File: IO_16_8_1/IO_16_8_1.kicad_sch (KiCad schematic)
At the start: 76 parts, among them J1 Conn_01x06, J2 nmount JST 1mm QWIIC, J3 nmount SW Debug, J4 USB_C_Receptacle_USB2.0, J5 Conn_01x06, SW1 Reset, SW2 Boot, SW3 SW_DIP_x04, U1 ADM3483, U2 W25Q32JVSS, U3 RP2040, U4 LMV321, U5 SN74AHCT1G125, U6 AP2112K-3.3, Y1 12MHz,18pF

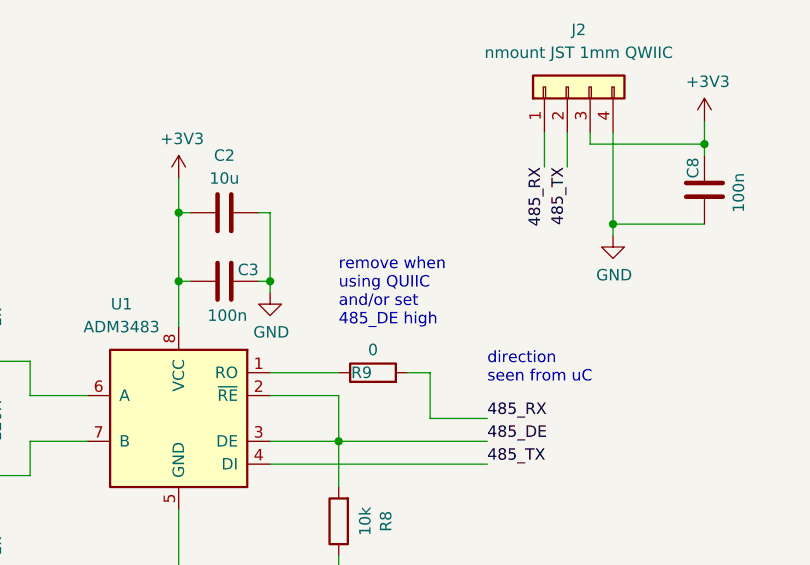
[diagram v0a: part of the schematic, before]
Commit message: fixed typo QUIIC -> QWIIC
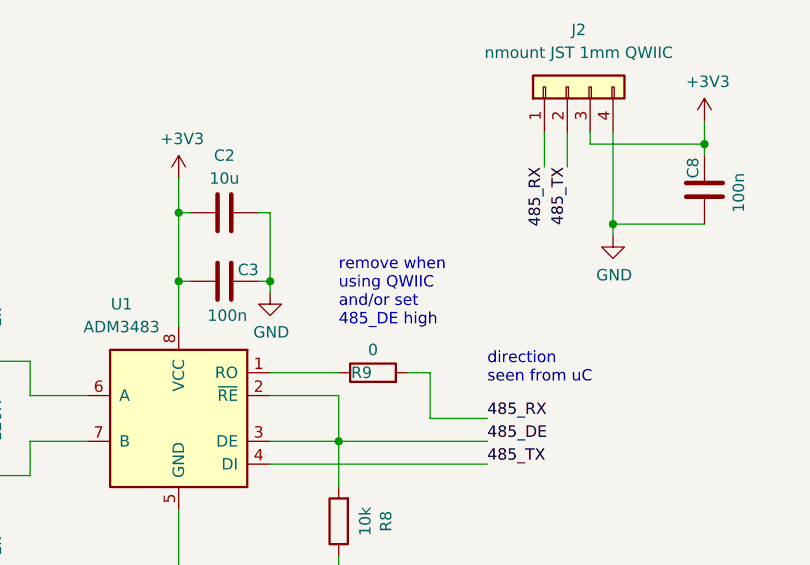
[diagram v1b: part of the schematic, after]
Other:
- note added: "remove when using QWIIC and/or set 485_DE high"
- note removed: "remove when using QUIIC and/or set 485_DE high"
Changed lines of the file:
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@@
     (effects (font (size 5 5) bold) (justify left bottom))
   )
-  (text "remove when\nusing QUIIC\nand/or set\n485_DE high" (at 105.41 50.8 0)
+  (text "remove when\nusing QWIIC\nand/or set\n485_DE high" (at 105.41 50.8 0)
     (effects (font (size 1.27 1.27)) (justify left bottom))
   )

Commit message: changed In_1, In_2
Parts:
- added R96, R97: 10k, symbol Device:R
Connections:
- net +3V3: now also R96.1, R97.1
- net 485_RX: now also R96.2
- net 485_TX: now also R97.2
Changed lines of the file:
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@@
     (rev "0.1")
   )
+  (junction (at 128.27 30.48) (diameter 0) (color 0 0 0 0)
+  )
   (junction (at 147.32 142.24) (diameter 0) (color 0 0 0 0)
   )
@@
   (junction (at 363.22 102.87) (diameter 0) (color 0 0 0 0)
   )
+  (junction (at 130.81 33.02) (diameter 0) (color 0 0 0 0)
+  )
   (junction (at 105.41 107.95) (diameter 0) (color 0 0 0 0)
   )
   (junction (at 46.99 67.31) (diameter 0) (color 0 0 0 0)
   )
+  (junction (at 114.3 30.48) (diameter 0) (color 0 0 0 0)
+  )
   (junction (at 135.89 39.37) (diameter 0) (color 0 0 0 0)
   )
@@
     (stroke (width 0) (type default) (color 0 0 0 0))
   )
+  (wire (pts (xy 114.3 33.02) (xy 114.3 30.48))
+    (stroke (width 0) (type default) (color 0 0 0 0))
+  )
   (wire (pts (xy 147.32 152.4) (xy 160.02 152.4))
     (stroke (width 0) (type default) (color 0 0 0 0))
@@
     (stroke (width 0) (type default) (color 0 0 0 0))
   )
-  (wire (pts (xy 128.27 29.21) (xy 128.27 33.02))
+  (wire (pts (xy 128.27 29.21) (xy 128.27 30.48))
     (stroke (width 0) (type default) (color 0 0 0 0))
   )
@@
     (stroke (width 0) (type default) (color 0 0 0 0))
   )
+  (wire (pts (xy 128.27 30.48) (xy 128.27 34.29))
+    (stroke (width 0) (type default) (color 0 0 0 0))
+  )
   (wire (pts (xy 220.98 167.64) (xy 227.33 167.64))
     (stroke (width 0) (type default) (color 0 0 0 0))
@@
     (stroke (width 0) (type default) (color 0 0 0 0))
   )
+  (wire (pts (xy 114.3 30.48) (xy 116.84 30.48))
+    (stroke (width 0) (type default) (color 0 0 0 0))
+  )
   (wire (pts (xy 175.26 52.07) (xy 175.26 54.61))
     (stroke (width 0) (type default) (color 0 0 0 0))
@@
     (stroke (width 0) (type default) (color 0 0 0 0))
   )
+  (wire (pts (xy 124.46 30.48) (xy 128.27 30.48))
+    (stroke (width 0) (type default) (color 0 0 0 0))
+  )
   (wire (pts (xy 233.68 214.63) (xy 233.68 227.33))
     (stroke (width 0) (type default) (color 0 0 0 0))
@@
     (stroke (width 0) (type default) (color 0 0 0 0))
   )
+  (wire (pts (xy 114.3 27.94) (xy 114.3 30.48))
+    (stroke (width 0) (type default) (color 0 0 0 0))
+  )
   (wire (pts (xy 360.68 110.49) (xy 360.68 115.57))
     (stroke (width 0) (type default) (color 0 0 0 0))
@@
     (stroke (width 0) (type default) (color 0 0 0 0))
   )
+  (wire (pts (xy 124.46 33.02) (xy 130.81 33.02))
+    (stroke (width 0) (type default) (color 0 0 0 0))
+  )
   (wire (pts (xy 90.17 209.55) (xy 99.06 209.55))
     (stroke (width 0) (type default) (color 0 0 0 0))
@@
     (stroke (width 0) (type default) (color 0 0 0 0))
   )
+  (wire (pts (xy 130.81 33.02) (xy 130.81 34.29))
+    (stroke (width 0) (type default) (color 0 0 0 0))
+  )
   (wire (pts (xy 182.88 63.5) (xy 190.5 63.5))
     (stroke (width 0) (type default) (color 0 0 0 0))
@@
     (stroke (width 0) (type default) (color 0 0 0 0))
   )
+  (wire (pts (xy 116.84 33.02) (xy 114.3 33.02))
+    (stroke (width 0) (type default) (color 0 0 0 0))
+  )
   (wire (pts (xy 363.22 105.41) (xy 365.76 105.41))
     (stroke (width 0) (type default) (color 0 0 0 0))
@@
     (effects (font (size 1.27 1.27)) (justify left bottom))
   )
-  (label "485_RX" (at 128.27 33.02 270)
+  (label "485_RX" (at 128.27 34.29 270)
     (effects (font (size 1.27 1.27)) (justify right bottom))
   )
@@
     (effects (font (size 1.27 1.27)) (justify left bottom))
   )
-  (label "485_TX" (at 130.81 33.02 270)
+  (label "485_TX" (at 130.81 34.29 270)
     (effects (font (size 1.27 1.27)) (justify right bottom))
   )
@@
     (pin "1")
   )
+  (symbol (lib_id "Device:R") (at 120.65 30.48 90) (unit 1)
+    (in_bom yes) (on_board yes)
+    (property "Reference" "R96" (id 0) (at 116.84 27.94 90))
+    (property "Value" "10k" (id 1) (at 121.92 27.94 90))
+    (property "Footprint" "" (id 2) (at 120.65 32.258 90)
+      (effects (font (size 1.27 1.27)) hide)
+    )
+    (property "Datasheet" "~" (id 3) (at 120.65 30.48 0)
+      (effects (font (size 1.27 1.27)) hide)
+    )
+    (pin "1")
+    (pin "2")
+  )
   (symbol (lib_id "Device:R") (at 182.88 209.55 0) (unit 1)
     (in_bom yes) (on_board yes) (fields_autoplaced)
@@
     (pin "2")
   )
+  (symbol (lib_id "Device:R") (at 120.65 33.02 90) (unit 1)
+    (in_bom yes) (on_board yes)
+    (property "Reference" "R97" (id 0) (at 116.84 35.56 90))
+    (property "Value" "10k" (id 1) (at 121.92 35.56 90))
+    (property "Footprint" "" (id 2) (at 120.65 34.798 90)
+      (effects (font (size 1.27 1.27)) hide)
+    )
+    (property "Datasheet" "~" (id 3) (at 120.65 33.02 0)
+      (effects (font (size 1.27 1.27)) hide)
+    )
+    (pin "1")
+    (pin "2")
+  )
   (symbol (lib_id "Device:C") (at 173.99 220.98 0) (unit 1)
     (in_bom yes) (on_board yes)
@@
   (symbol (lib_id "logo:LOGO") (at 307.34 261.62 0) (unit 1)
     (in_bom yes) (on_board yes) (fields_autoplaced)
-    (property "Reference" "#G?" (id 0) (at 307.34 254.7529 0)
+    (property "Reference" "#G1" (id 0) (at 307.34 254.7529 0)
       (effects (font (size 1.27 1.27)) hide)
     )
@@
     (pin "1")
   )
+  (symbol (lib_id "power:+3V3") (at 114.3 27.94 0) (unit 1)
+    (in_bom yes) (on_board yes)
+    (property "Reference" "#PWR02" (id 0) (at 114.3 31.75 0)
+      (effects (font (size 1.27 1.27)) hide)
+    )
+    (property "Value" "+3V3" (id 1) (at 114.681 23.5458 0))
+    (property "Footprint" "" (id 2) (at 114.3 27.94 0)
+      (effects (font (size 1.27 1.27)) hide)
+    )
+    (property "Datasheet" "" (id 3) (at 114.3 27.94 0)
+      (effects (font (size 1.27 1.27)) hide)
+    )
+    (pin "1")
+  )
   (symbol (lib_id "power:GND") (at 198.12 227.33 0) (unit 1)
     (in_bom yes) (on_board yes)
@@
   (symbol_instances
     (path "/53a203ba-73f4-4cb7-ac18-a001836c85e7"
-      (reference "#G?") (unit 1) (value "LOGO") (footprint "")
-    )
-    (path "/c5f8e297-f0f5-428a-9eba-1c51bb8e36a7/a265258b-b67b-40d7-af50-860ef40072e1"
-      (reference "#G?") (unit 1) (value "LOGO") (footprint "")
+      (reference "#G1") (unit 1) (value "LOGO") (footprint "")
     )
     (path "/e4dc0cf8-90a8-459a-87df-3f71f348298f/df026378-0be4-43ae-9a9f-c6ac47fc6570"
-      (reference "#G?") (unit 1) (value "LOGO") (footprint "")
+      (reference "#G2") (unit 1) (value "LOGO") (footprint "")
+    )
+    (path "/c5f8e297-f0f5-428a-9eba-1c51bb8e36a7/a265258b-b67b-40d7-af50-860ef40072e1"
+      (reference "#G3") (unit 1) (value "LOGO") (footprint "")
     )
     (path "/0b693a2d-a2e7-4a59-abfe-11ff07890c2f"
       (reference "#PWR01") (unit 1) (value "GND") (footprint "")
     )
+    (path "/ac973ff1-f752-4c46-8c19-073be36f5fc4"
+      (reference "#PWR02") (unit 1) (value "+3V3") (footprint "")
+    )
+    (path "/e4dc0cf8-90a8-459a-87df-3f71f348298f/d125a507-89f4-4840-838f-5e754df6ec9e"
+      (reference "#PWR03") (unit 1) (value "+3V3") (footprint "")
+    )
+    (path "/e4dc0cf8-90a8-459a-87df-3f71f348298f/c16576ae-67c9-4af0-bbd2-9ca7bc198a01"
+      (reference "#PWR04") (unit 1) (value "+3V3") (footprint "")
+    )
     (path "/cd816392-78de-4c49-bac0-ed4e8ab59e24"
       (reference "#PWR0101") (unit 1) (value "GND") (footprint "")
@@
     )
     (path "/e4dc0cf8-90a8-459a-87df-3f71f348298f/68f7c5d7-a1d2-48f6-ab5b-316284d09c42"
-      (reference "C28") (unit 1) (value "470p") (footprint "Capacitor_SMD:C_0603_1608Metric")
+      (reference "C28") (unit 1) (value "nmount") (footprint "Capacitor_SMD:C_0603_1608Metric")
     )
     (path "/e4dc0cf8-90a8-459a-87df-3f71f348298f/6196ef9b-97ef-4ca7-a79c-491f2af658e2"
-      (reference "C29") (unit 1) (value "470p") (footprint "Capacitor_SMD:C_0603_1608Metric")
+      (reference "C29") (unit 1) (value "nmount") (footprint "Capacitor_SMD:C_0603_1608Metric")
     )
     (path "/e4dc0cf8-90a8-459a-87df-3f71f348298f/de507796-11bd-4d03-8a6c-ef10a63305e1"
@@
     )
     (path "/e4dc0cf8-90a8-459a-87df-3f71f348298f/e58e7d5e-dfe2-4520-82eb-f98edb15e68c"
-      (reference "R33") (unit 1) (value "10k") (footprint "Resistor_SMD:R_0603_1608Metric")
+      (reference "R33") (unit 1) (value "3k") (footprint "Resistor_SMD:R_0603_1608Metric")
     )
     (path "/e4dc0cf8-90a8-459a-87df-3f71f348298f/51f998a1-fc94-4244-a9be-e066f66d9214"
-      (reference "R34") (unit 1) (value "10k") (footprint "Resistor_SMD:R_0603_1608Metric")
+      (reference "R34") (unit 1) (value "3k") (footprint "Resistor_SMD:R_0603_1608Metric")
     )
     (path "/e4dc0cf8-90a8-459a-87df-3f71f348298f/f1fb512a-540a-439e-adb6-adfb11f8472e"
@@
     )
     (path "/e4dc0cf8-90a8-459a-87df-3f71f348298f/8f24e08b-b68f-4051-a27c-5020dc8c0b9b"
-      (reference "R39") (unit 1) (value "10k") (footprint "Resistor_SMD:R_0603_1608Metric")
+      (reference "R39") (unit 1) (value "3k") (footprint "Resistor_SMD:R_0603_1608Metric")
     )
     (path "/e4dc0cf8-90a8-459a-87df-3f71f348298f/8c743843-4a0e-4e33-8885-c57e039fd74b"
-      (reference "R40") (unit 1) (value "10k") (footprint "Resistor_SMD:R_0603_1608Metric")
+      (reference "R40") (unit 1) (value "3k") (footprint "Resistor_SMD:R_0603_1608Metric")
     )
     (path "/e4dc0cf8-90a8-459a-87df-3f71f348298f/0c8c43cf-13e7-4c55-90c2-6a7ce5701b2e"
@@
       (reference "R95") (unit 1) (value "100R") (footprint "Resistor_SMD:R_0603_1608Metric")
     )
+    (path "/0c6847b7-0130-4cc6-9f95-1d6921632bde"
+      (reference "R96") (unit 1) (value "10k") (footprint "")
+    )
+    (path "/2820d80e-b6a9-4476-9d77-3cd017a4f6be"
+      (reference "R97") (unit 1) (value "10k") (footprint "")
+    )
+    (path "/e4dc0cf8-90a8-459a-87df-3f71f348298f/1843d60f-2cb6-4ea4-a96b-eec8acf9592e"
+      (reference "R98") (unit 1) (value "nmount") (footprint "Resistor_SMD:R_0603_1608Metric")
+    )
+    (path "/e4dc0cf8-90a8-459a-87df-3f71f348298f/244fcc3e-e487-40af-82db-1dcb3b6052df"
+      (reference "R99") (unit 1) (value "nmount") (footprint "Resistor_SMD:R_0603_1608Metric")
+    )
     (path "/3855f2d1-da08-4c4c-9f73-2b65f7451c29"

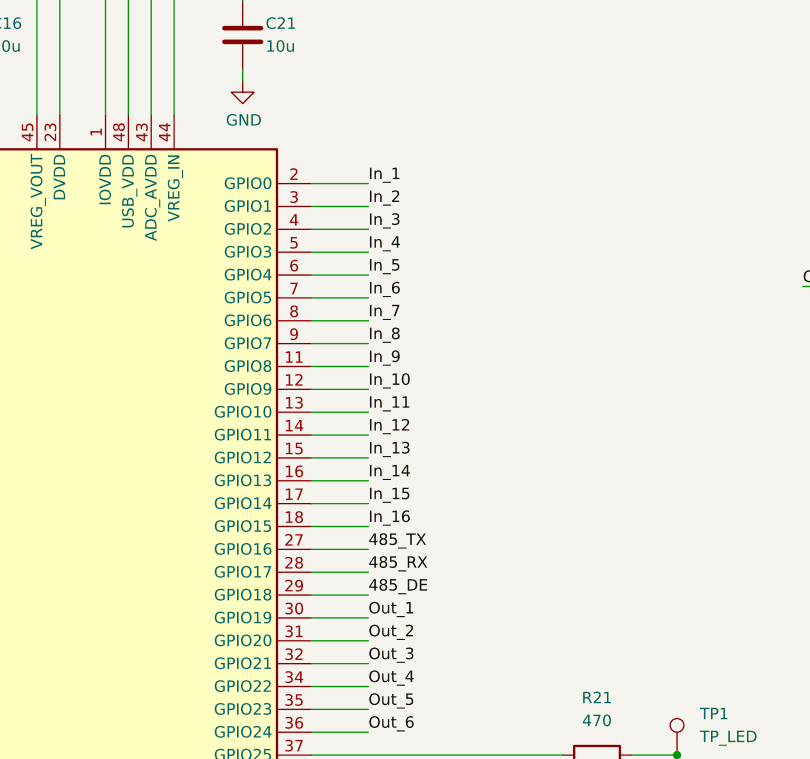
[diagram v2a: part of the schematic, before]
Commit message: different pins for RS485
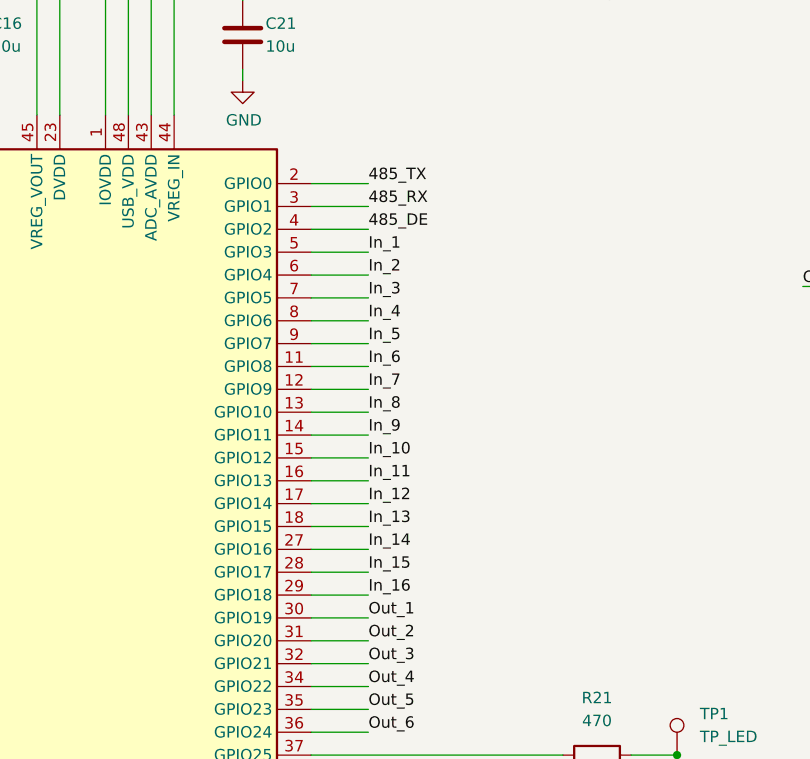
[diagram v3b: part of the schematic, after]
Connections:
- net 485_DE: now also U3.4 (GPIO2); no longer U3.29 (GPIO18)
- net 485_RX: now also U3.3 (GPIO1); no longer U3.28 (GPIO17)
- net 485_TX: now also U3.2 (GPIO0); no longer U3.27 (GPIO16)
- net In_1: now also U3.5 (GPIO3); no longer U3.2 (GPIO0)
- net In_10: now also U3.15 (GPIO12); no longer U3.12 (GPIO9)
- net In_11: now also U3.16 (GPIO13); no longer U3.13 (GPIO10)
- net In_12: now also U3.17 (GPIO14); no longer U3.14 (GPIO11)
- net In_13: now also U3.18 (GPIO15); no longer U3.15 (GPIO12)
- net In_14: now also U3.27 (GPIO16); no longer U3.16 (GPIO13)
- net In_15: now also U3.28 (GPIO17); no longer U3.17 (GPIO14)
- net In_16: now also U3.29 (GPIO18); no longer U3.18 (GPIO15)
- net In_2: now also U3.6 (GPIO4); no longer U3.3 (GPIO1)
- net In_3: now also U3.7 (GPIO5); no longer U3.4 (GPIO2)
- net In_4: now also U3.8 (GPIO6); no longer U3.5 (GPIO3)
- net In_5: now also U3.9 (GPIO7); no longer U3.6 (GPIO4)
- net In_6: now also U3.11 (GPIO8); no longer U3.7 (GPIO5)
- net In_7: now also U3.12 (GPIO9); no longer U3.8 (GPIO6)
- net In_8: now also U3.13 (GPIO10); no longer U3.9 (GPIO7)
- net In_9: now also U3.14 (GPIO11); no longer U3.11 (GPIO8)

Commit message: PCB init
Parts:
- C6, C7: footprint (none) -> Capacitor_SMD:C_0603_1608Metric
- D3: footprint (none) -> LED_SMD:LED_0805_2012Metric
- J1, J5: footprint RTMPin_CAE:Terminal_Block_RTMPin -> IO_16_8_1:Terminal_Block_RTMPin
- J2: footprint (none) -> Connector_JST:JST_SH_SM04B-SRSS-TB_1x04-1MP_P1.00mm_Horizontal
- J3: footprint (none) -> Connector_PinSocket_2.54mm:PinSocket_1x03_P2.54mm_Vertical
- J4: footprint (none) -> Connector_USB:USB_C_Receptacle_XKB_U262-16XN-4BVC11
- R10, R11, R12, R13, R14, R16, R17, R18, R19, R20, R21, R22, R23, R24, R25, R6, R7, R9, R96, R97: footprint (none) -> Resistor_SMD:R_0603_1608Metric
- SW1, SW2: footprint (none) -> Button_Switch_SMD:SW_SPST_SKQG_WithStem
- SW3: footprint (none) -> Button_Switch_SMD:SW_DIP_SPSTx04_Slide_6.7x11.72mm_W8.61mm_P2.54mm_LowProfile
- U4: footprint (none) -> Package_TO_SOT_SMD:SOT-23-5

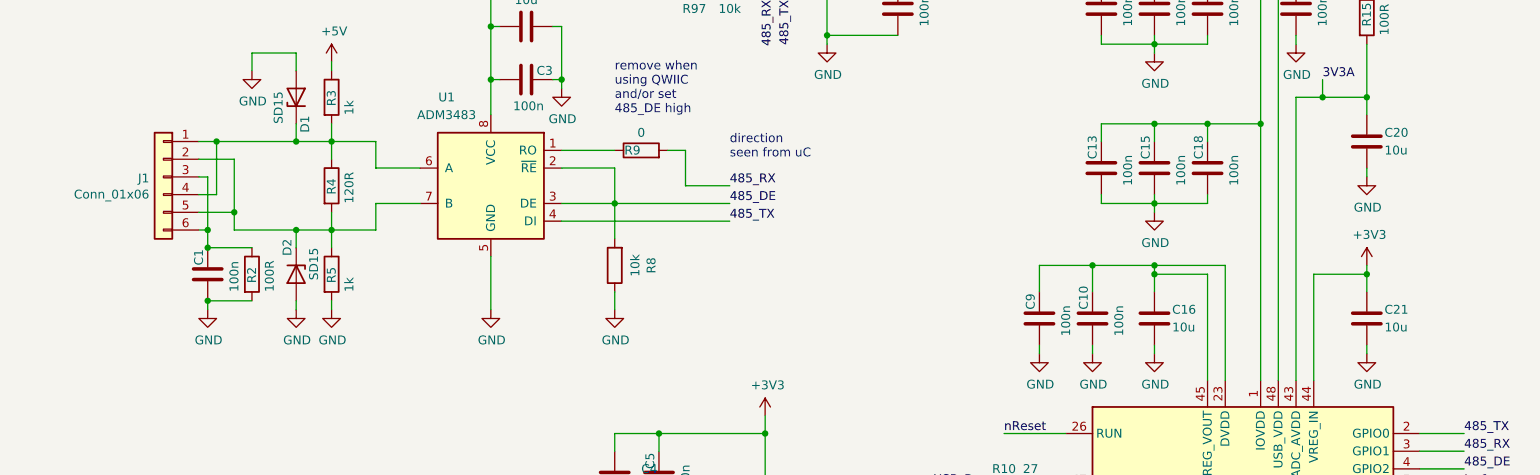
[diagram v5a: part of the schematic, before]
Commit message: smaller Cs
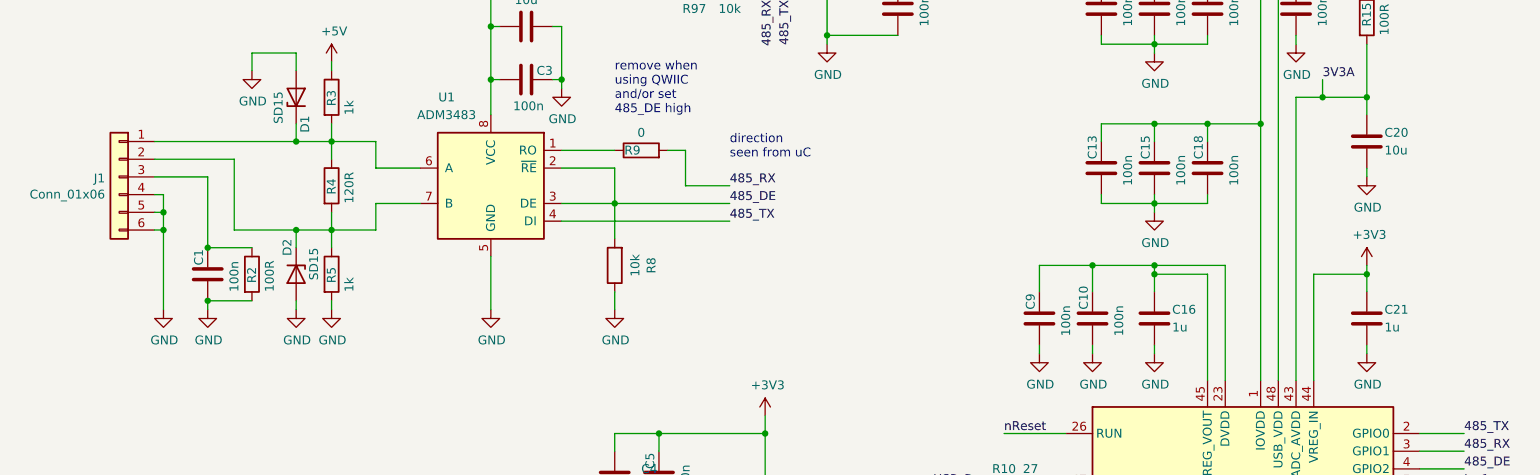
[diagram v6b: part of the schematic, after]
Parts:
- C1, C10, C11, C12, C13, C14, C15, C17, C18, C19, C22, C24, C27, C3, C5, C6, C7, C8, C9: footprint Capacitor_SMD:C_0603_1608Metric -> Capacitor_SMD:C_0402_1005Metric
- C16, C21: value 10u -> 1u; footprint Capacitor_SMD:C_0603_1608Metric -> Capacitor_SMD:C_0402_1005Metric
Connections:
- net GND: now also J1.4 (Pin_4), J1.5 (Pin_5), J1.6 (Pin_6)
- net at C1.1, J1.3 (Pin_3), R2.1: no longer J1.6 (Pin_6)
- net at D1.1 (K), J1.1 (Pin_1), R3.2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: no longer J1.4 (Pin_4)
- net at D2.1 (K), J1.2 (Pin_2), R4.2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: no longer J1.5 (Pin_5)
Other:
- moved on the sheet: J1

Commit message: 1/2 routed
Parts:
- removed C18: 100n, Capacitor_SMD:C_0402_1005Metric, symbol Device:C
- C19: Note may be together with C at pin 49 -> together with C at pin 49
- D4: value 3A SMA -> 1A; footprint Diode_SMD:D_SMA -> Diode_SMD:D_SOD-323
- R10, R11, R12, R16, R20, R3, R5, R6: footprint Resistor_SMD:R_0603_1608Metric -> Resistor_SMD:R_0402_1005Metric
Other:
- moved on the sheet: C13, C15

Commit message: routed
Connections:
- net 1V1: now reaches C10.1, C16.1, C9.1, U3.23 (DVDD), U3.45 (VREG_VOUT), U3.50 (DVDD)
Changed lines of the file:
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@@
+    (stroke (width 0) (type default) (color 0 0 0 0))
+  )
+  (wire (pts (xy 173.99 69.85) (xy 173.99 72.39))
     (stroke (width 0) (type default) (color 0 0 0 0))
   )
@@
     (effects (font (size 1.27 1.27)) (justify left bottom))
   )
+  (label "1V1" (at 173.99 69.85 0)
+    (effects (font (size 1.27 1.27)) (justify left bottom))
+  )
